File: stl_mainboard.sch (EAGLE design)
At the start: 5 parts, among them IC1 LM555D

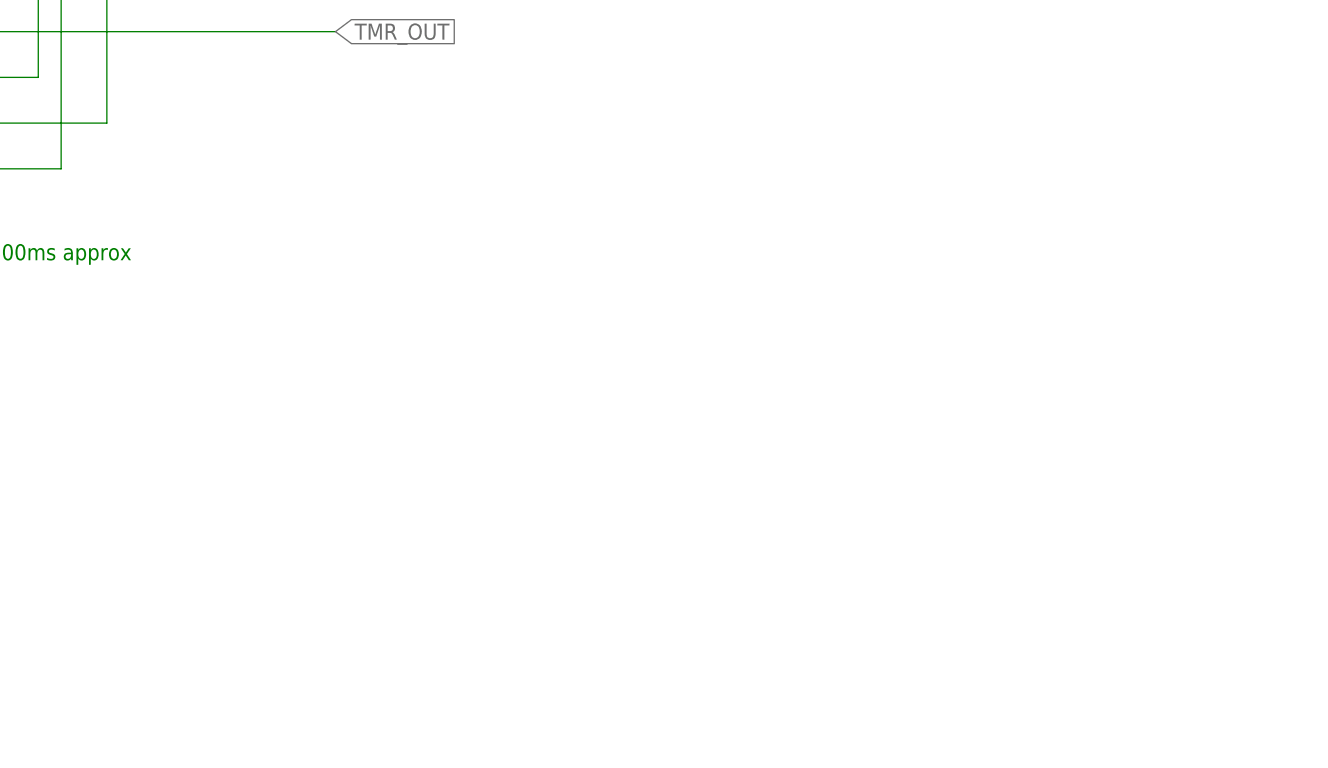
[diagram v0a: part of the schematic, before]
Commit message: Adds basicaly 555 timer schematic for 300ms period TODO: * develop 5V power supply * develop revers voltage protection * develop fuse * develop antistatic protection * develop MOSFET-base load control
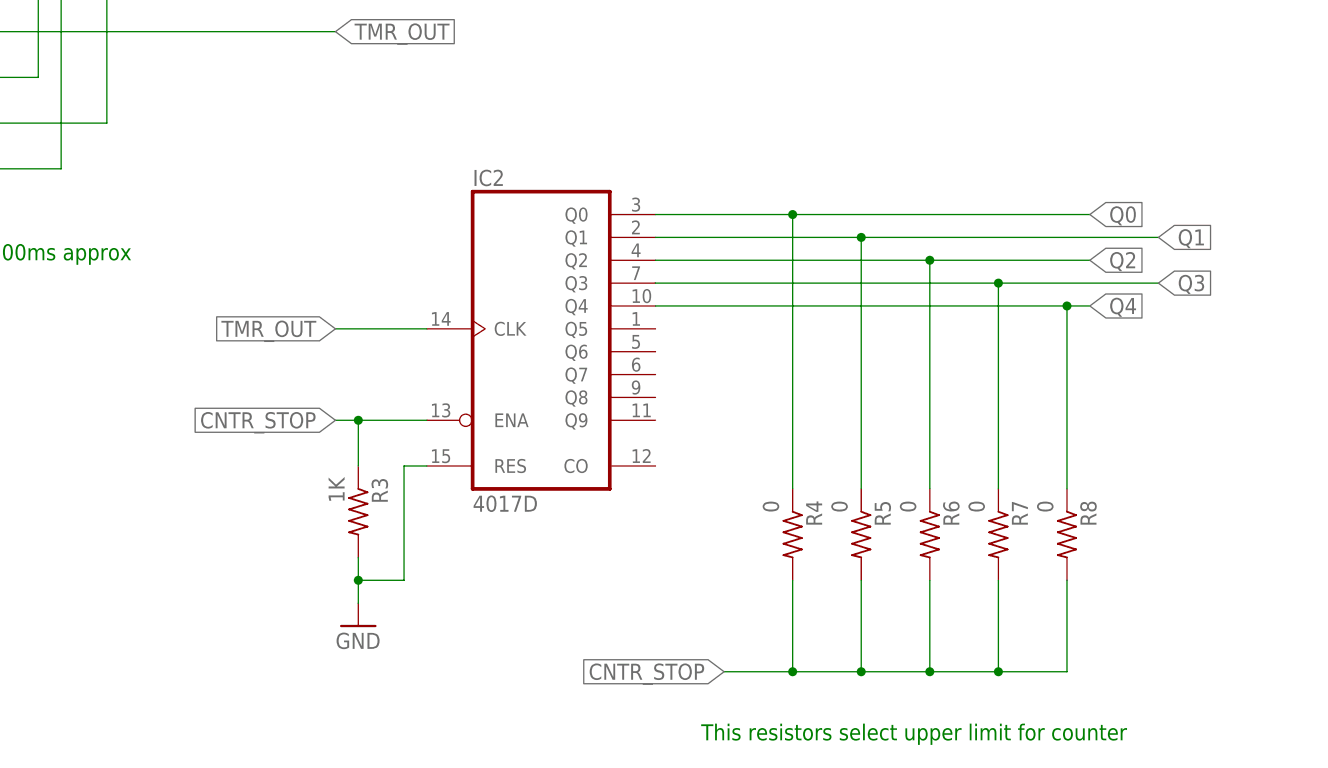
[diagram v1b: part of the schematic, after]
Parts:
- added IC2: 4017D, 40xx:4017D
- added R3: 1K, rcl:R-US_M1206
- added R4, R5, R6, R7, R8: 0, rcl:R-US_M1206
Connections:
- net +5V renamed VDD
- new net CNTR_STOP: IC2A.ENA, R3.1, R4.2, R5.2, R6.2, R7.2, R8.2
- new net Q0: IC2A.Q0, R4.1
- new net Q1: IC2A.Q1, R5.1
- new net Q2: IC2A.Q2, R6.1
- new net Q3: IC2A.Q3, R7.1
- new net Q4: IC2A.Q4, R8.1
- new net VSS: C1.-, C2.2, IC1.GND
- net GND: now also IC2A.RES, R3.2; no longer C1.-, C2.2, IC1.GND
- net TMR_OUT: now also IC2A.CLK
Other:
- note added: "This resistors select upper limit for counter"
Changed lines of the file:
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@@
 <part name="R1" library="rcl" deviceset="R-US_" device="M1206" value="1K"/>
 <part name="R2" library="rcl" deviceset="R-US_" device="M1206" value="4K2"/>
+<part name="IC2" library="40xx" deviceset="4017" device="D"/>
+<part name="R3" library="rcl" deviceset="R-US_" device="M1206" value="1K"/>
+<part name="GND2" library="supply1" deviceset="GND" device=""/>
+<part name="R4" library="rcl" deviceset="R-US_" device="M1206" value="0"/>
+<part name="R5" library="rcl" deviceset="R-US_" device="M1206" value="0"/>
+<part name="R6" library="rcl" deviceset="R-US_" device="M1206" value="0"/>
+<part name="R7" library="rcl" deviceset="R-US_" device="M1206" value="0"/>
+<part name="R8" library="rcl" deviceset="R-US_" device="M1206" value="0"/>
 </parts>
 <sheets>
@@
 <plain>
 <text x="-5.08" y="33.02" size="1.778" layer="91">Tiimer period must be 300ms approx</text>
+<text x="99.06" y="-20.32" size="1.778" layer="91">This resistors select upper limit for counter</text>
 </plain>
 <instances>
@@
 <instance part="R1" gate="G$1" x="5.08" y="76.2" rot="R180"/>
 <instance part="R2" gate="G$1" x="5.08" y="66.04" rot="R180"/>
+<instance part="IC2" gate="A" x="81.28" y="25.4"/>
+<instance part="R3" gate="G$1" x="60.96" y="5.08" rot="R270"/>
+<instance part="GND2" gate="1" x="60.96" y="-7.62"/>
+<instance part="R4" gate="G$1" x="109.22" y="2.54" rot="R270"/>
+<instance part="R5" gate="G$1" x="116.84" y="2.54" rot="R270"/>
+<instance part="R6" gate="G$1" x="124.46" y="2.54" rot="R270"/>
+<instance part="R7" gate="G$1" x="132.08" y="2.54" rot="R270"/>
+<instance part="R8" gate="G$1" x="139.7" y="2.54" rot="R270"/>
 </instances>
 <busses>
 </busses>
 <nets>
-<net name="+5V" class="0">
+<net name="VDD" class="0">
 <segment>
 <pinref part="P+2" gate="1" pin="+5V"/>
@@
 </segment>
 </net>
-<net name="GND" class="0">
+<net name="VSS" class="0">
 <segment>
 <pinref part="GND1" gate="1" pin="GND"/>
@@
 <wire x1="17.78" y1="58.42" x2="58.42" y2="58.42" width="0.1524" layer="91"/>
 <label x="58.42" y="58.42" size="1.778" layer="95" xref="yes"/>
+</segment>
+<segment>
+<pinref part="IC2" gate="A" pin="CLK"/>
+<wire x1="68.58" y1="25.4" x2="58.42" y2="25.4" width="0.1524" layer="91"/>
+<label x="58.42" y="25.4" size="1.778" layer="95" rot="R180" xref="yes"/>
 </segment>
 </net>
@@
 </segment>
 </net>
+<net name="CNTR_STOP" class="0">
+<segment>
+<pinref part="IC2" gate="A" pin="ENA"/>
+<pinref part="R3" gate="G$1" pin="1"/>
+<wire x1="68.58" y1="15.24" x2="60.96" y2="15.24" width="0.1524" layer="91"/>
+<wire x1="60.96" y1="15.24" x2="60.96" y2="10.16" width="0.1524" layer="91"/>
+<wire x1="60.96" y1="15.24" x2="58.42" y2="15.24" width="0.1524" layer="91"/>
+<label x="58.42" y="15.24" size="1.778" layer="95" rot="R180" xref="yes"/>
+<junction x="60.96" y="15.24"/>
+</segment>
+<segment>
+<pinref part="R8" gate="G$1" pin="2"/>
+<wire x1="139.7" y1="-2.54" x2="139.7" y2="-12.7" width="0.1524" layer="91"/>
+<wire x1="139.7" y1="-12.7" x2="132.08" y2="-12.7" width="0.1524" layer="91"/>
+<pinref part="R4" gate="G$1" pin="2"/>
+<wire x1="132.08" y1="-12.7" x2="124.46" y2="-12.7" width="0.1524" layer="91"/>
+<wire x1="124.46" y1="-12.7" x2="116.84" y2="-12.7" width="0.1524" layer="91"/>
+<wire x1="116.84" y1="-12.7" x2="109.22" y2="-12.7" width="0.1524" layer="91"/>
+<wire x1="109.22" y1="-12.7" x2="101.6" y2="-12.7" width="0.1524" layer="91"/>
+<wire x1="109.22" y1="-2.54" x2="109.22" y2="-12.7" width="0.1524" layer="91"/>
+<pinref part="R5" gate="G$1" pin="2"/>
+<wire x1="116.84" y1="-2.54" x2="116.84" y2="-12.7" width="0.1524" layer="91"/>
+<pinref part="R6" gate="G$1" pin="2"/>
+<wire x1="124.46" y1="-2.54" x2="124.46" y2="-12.7" width="0.1524" layer="91"/>
+<pinref part="R7" gate="G$1" pin="2"/>
+<wire x1="132.08" y1="-2.54" x2="132.08" y2="-12.7" width="0.1524" layer="91"/>
+<junction x="109.22" y="-12.7"/>
+<junction x="116.84" y="-12.7"/>
+<junction x="124.46" y="-12.7"/>
+<junction x="132.08" y="-12.7"/>
+<label x="101.6" y="-12.7" size="1.778" layer="95" rot="R180" xref="yes"/>
+</segment>
+</net>
+<net name="GND" class="0">
+<segment>
+<pinref part="R3" gate="G$1" pin="2"/>
+<pinref part="GND2" gate="1" pin="GND"/>
+<wire x1="60.96" y1="0" x2="60.96" y2="-2.54" width="0.1524" layer="91"/>
+<pinref part="IC2" gate="A" pin="RES"/>
+<wire x1="60.96" y1="-2.54" x2="60.96" y2="-5.08" width="0.1524" layer="91"/>
+<wire x1="68.58" y1="10.16" x2="66.04" y2="10.16" width="0.1524" layer="91"/>
+<wire x1="66.04" y1="10.16" x2="66.04" y2="-2.54" width="0.1524" layer="91"/>
+<wire x1="66.04" y1="-2.54" x2="60.96" y2="-2.54" width="0.1524" layer="91"/>
+<junction x="60.96" y="-2.54"/>
+</segment>
+</net>
+<net name="Q0" class="0">
+<segment>
+<pinref part="IC2" gate="A" pin="Q0"/>
+<wire x1="93.98" y1="38.1" x2="109.22" y2="38.1" width="0.1524" layer="91"/>
+<pinref part="R4" gate="G$1" pin="1"/>
+<wire x1="109.22" y1="7.62" x2="109.22" y2="38.1" width="0.1524" layer="91"/>
+<junction x="109.22" y="38.1"/>
+<wire x1="109.22" y1="38.1" x2="142.24" y2="38.1" width="0.1524" layer="91"/>
+<label x="142.24" y="38.1" size="1.778" layer="95" xref="yes"/>
+</segment>
+</net>
+<net name="Q1" class="0">
+<segment>
+<pinref part="IC2" gate="A" pin="Q1"/>
+<wire x1="93.98" y1="35.56" x2="116.84" y2="35.56" width="0.1524" layer="91"/>
+<pinref part="R5" gate="G$1" pin="1"/>
+<wire x1="116.84" y1="7.62" x2="116.84" y2="35.56" width="0.1524" layer="91"/>
+<junction x="116.84" y="35.56"/>
+<wire x1="116.84" y1="35.56" x2="149.86" y2="35.56" width="0.1524" layer="91"/>
+<label x="149.86" y="35.56" size="1.778" layer="95" xref="yes"/>
+</segment>
+</net>
+<net name="Q2" class="0">
+<segment>
+<pinref part="IC2" gate="A" pin="Q2"/>
+<wire x1="93.98" y1="33.02" x2="124.46" y2="33.02" width="0.1524" layer="91"/>
+<pinref part="R6" gate="G$1" pin="1"/>
+<wire x1="124.46" y1="7.62" x2="124.46" y2="33.02" width="0.1524" layer="91"/>
+<junction x="124.46" y="33.02"/>
+<wire x1="124.46" y1="33.02" x2="142.24" y2="33.02" width="0.1524" layer="91"/>
+<label x="142.24" y="33.02" size="1.778" layer="95" xref="yes"/>
+</segment>
+</net>
+<net name="Q3" class="0">
+<segment>
+<pinref part="IC2" gate="A" pin="Q3"/>
+<wire x1="93.98" y1="30.48" x2="132.08" y2="30.48" width="0.1524" layer="91"/>
+<pinref part="R7" gate="G$1" pin="1"/>
+<wire x1="132.08" y1="7.62" x2="132.08" y2="30.48" width="0.1524" layer="91"/>
+<junction x="132.08" y="30.48"/>
+<wire x1="132.08" y1="30.48" x2="149.86" y2="30.48" width="0.1524" layer="91"/>
+<label x="149.86" y="30.48" size="1.778" layer="95" xref="yes"/>
+</segment>
+</net>
+<net name="Q4" class="0">
+<segment>
+<pinref part="IC2" gate="A" pin="Q4"/>
+<wire x1="93.98" y1="27.94" x2="139.7" y2="27.94" width="0.1524" layer="91"/>
+<pinref part="R8" gate="G$1" pin="1"/>
+<wire x1="139.7" y1="27.94" x2="142.24" y2="27.94" width="0.1524" layer="91"/>
+<wire x1="139.7" y1="7.62" x2="139.7" y2="27.94" width="0.1524" layer="91"/>
+<junction x="139.7" y="27.94"/>
+<label x="142.24" y="27.94" size="1.778" layer="95" xref="yes"/>
+</segment>
+</net>

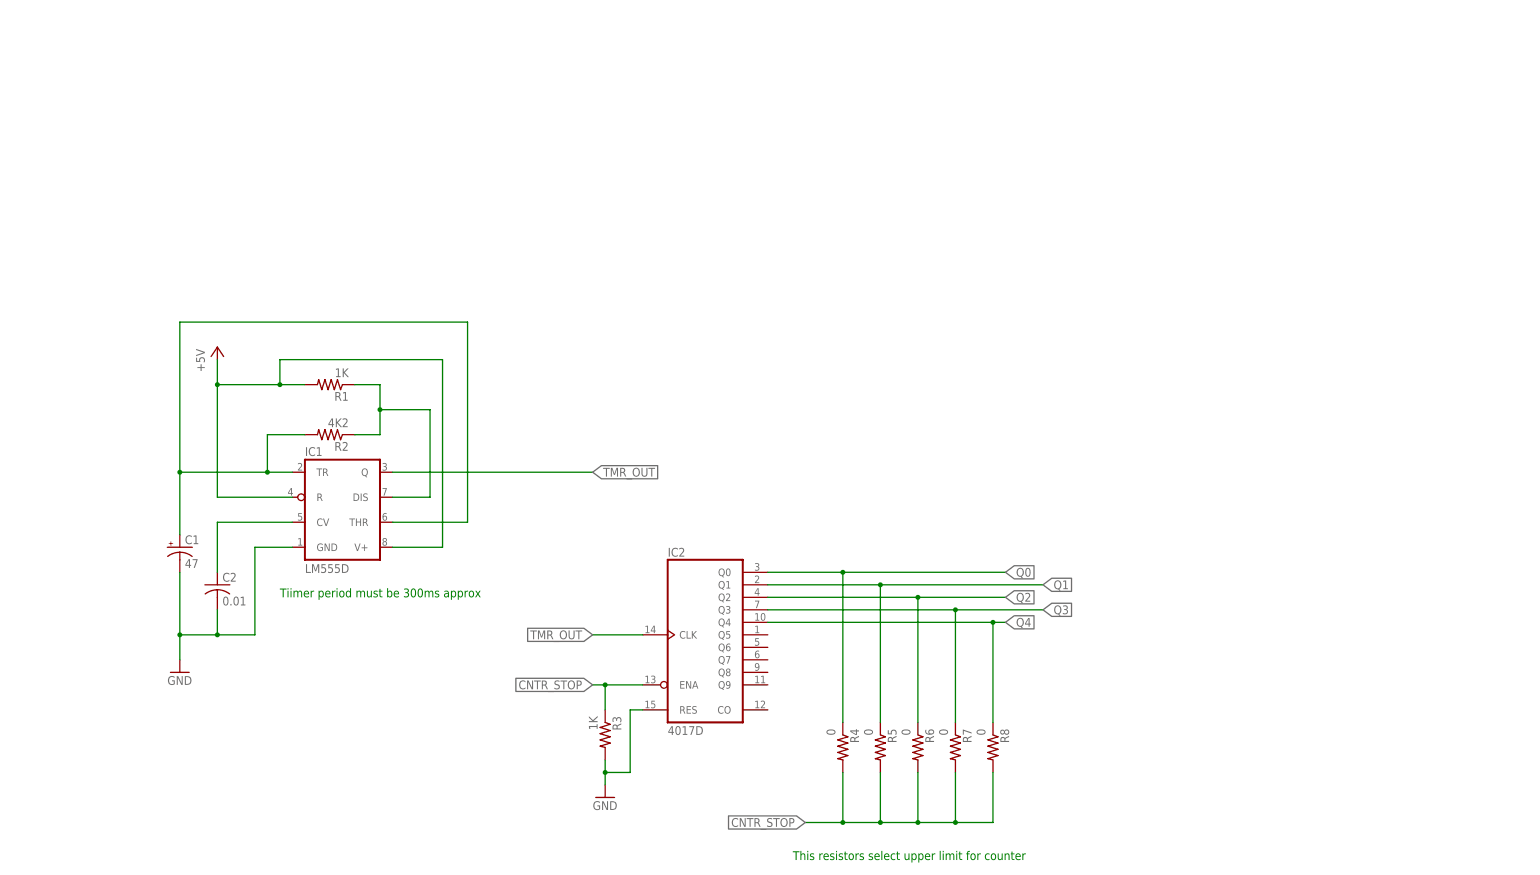
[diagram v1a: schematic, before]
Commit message: Adds power mosfets, removes unnecessary 7805 TODO: * develop revers voltage protection * develop fuse * develop antistatic protection
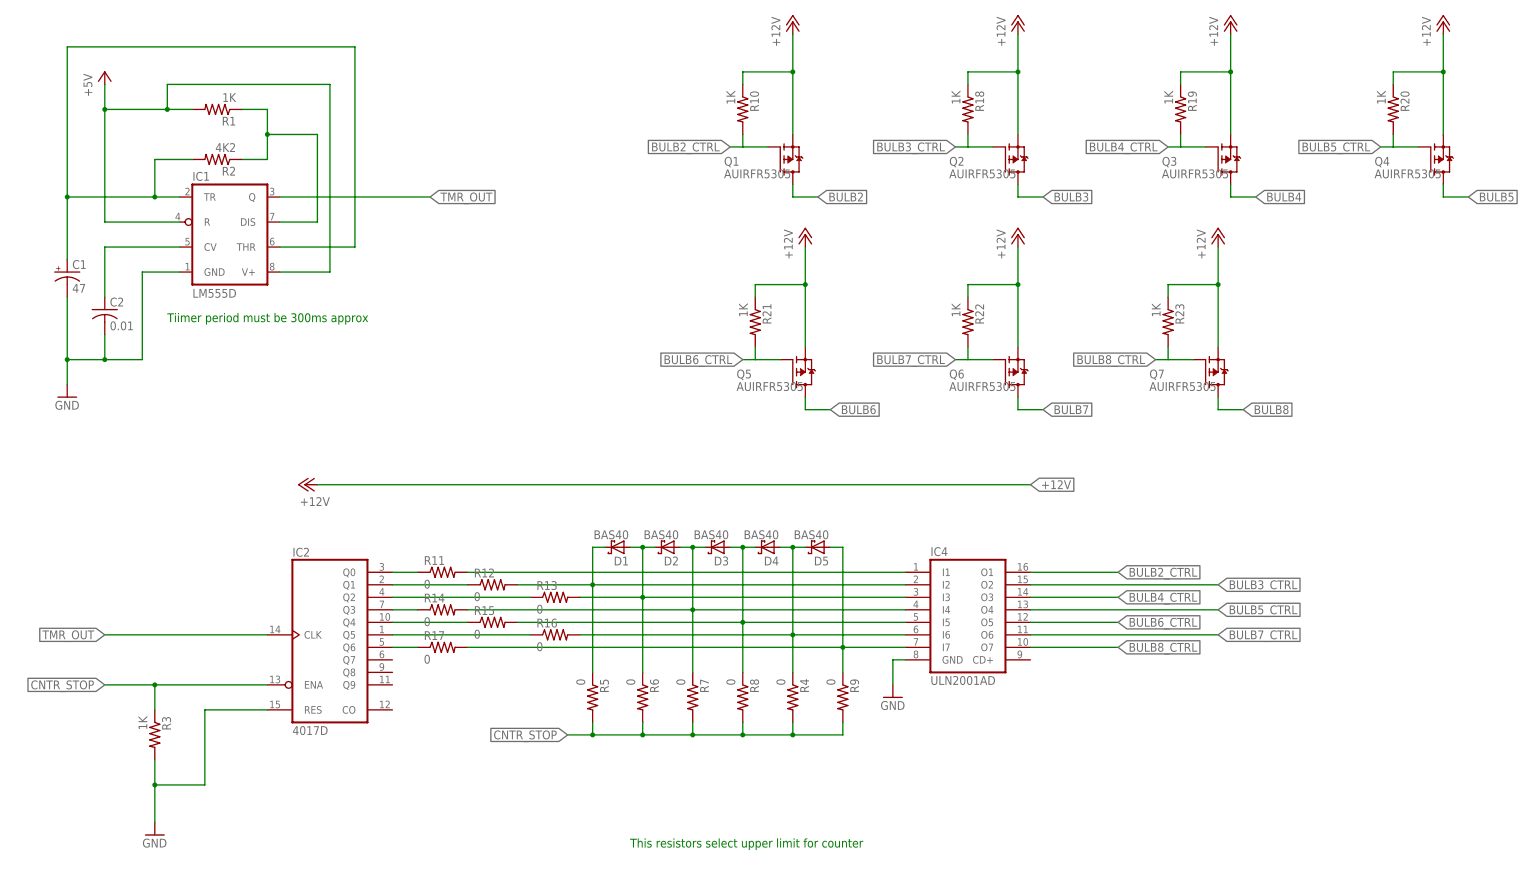
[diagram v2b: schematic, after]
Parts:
- added D1, D2, D3, D4, D5: BAS40, diode:BAS40
- added IC4: ULN2001AD, uln-udn:ULN2001AD
- added Q1, Q2, Q3, Q4, Q5, Q6, Q7: AUIRFR5305, transistor-fet:SPD30P06PTO252
- added R10, R18, R19, R20, R21, R22, R23: 1K, rcl:R-US_M1206
- added R11, R12, R13, R14, R15, R16, R17, R9: 0, rcl:R-US_M1206
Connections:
- new net +12V: Q1.S, Q2.S, Q3.S, Q4.S, Q5.S, Q6.S, Q7.S, R10.1, R18.1, R19.1, R20.1, R21.1, R22.1, R23.1
- new net BULB2: Q1.D
- new net BULB2_CTRL: IC4.O1, Q1.G, R10.2
- new net BULB3: Q2.D
- new net BULB3_CTRL: IC4.O2, Q2.G, R18.2
- new net BULB4: Q3.D
- new net BULB4_CTRL: IC4.O3, Q3.G, R19.2
- new net BULB5: Q4.D
- new net BULB5_CTRL: IC4.O4, Q4.G, R20.2
- new net BULB6: Q5.D
- new net BULB6_CTRL: IC4.O5, Q5.G, R21.2
- new net BULB7: Q6.D
- new net BULB7_CTRL: IC4.O6, Q6.G, R22.2
- new net BULB8: Q7.D
- new net BULB8_CTRL: IC4.O7, Q7.G, R23.2
- new net N$10: IC2A.Q6, R17.1
- new net N$4: IC2A.Q0, R11.1
- new net N$5: IC2A.Q1, R12.1
- new net N$6: IC2A.Q2, R13.1
- new net N$7: IC2A.Q3, R14.1
- new net N$8: IC2A.Q4, R15.1
- new net N$9: IC2A.Q5, R16.1
- new net Q5: D4.A, D5.C, IC4.I6, R16.2, R4.1
- new net Q6: D5.A, IC4.I7, R17.2, R9.1
- net CNTR_STOP: now also R9.2
- net GND: now also IC4.GND
- net Q0: now also IC4.I1, R11.2; no longer IC2A.Q0, R4.1
- net Q1: now also D1.C, IC4.I2, R12.2; no longer IC2A.Q1
- net Q2: now also D1.A, D2.C, IC4.I3, R13.2; no longer IC2A.Q2
- net Q3: now also D2.A, D3.C, IC4.I4, R14.2; no longer IC2A.Q3
- net Q4: now also D3.A, D4.C, IC4.I5, R15.2; no longer IC2A.Q4
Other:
- moved on the sheet: C1, C2, IC1, IC2, R1, R2, R3, R4, R5, R6, R7, R8

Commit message: WIP: input voltage spike and reverse protection
Also adds wago 508 screw connectors

TODO:
* develop fuse
* develop antistatic protection
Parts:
- added C3: 0.1uF, rcl:C-USC1206
- added D6: SMBJ15, diode:SUPPRESSOR-SMBJ
- added D7: 48CTQ060S, diode:BY229B
- added X1: (no value), con-wago-500:W237-102
- added X2: (no value), con-wago-508:W237-08P
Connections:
- new net N$11: D7.2, X1-1.KL
- net +12V: now also D6.C, D7.1, D7.K
- net GND: now also D6.A, X1-2.KL
- net VDD: now also C3.1
- net VSS: now also C3.2
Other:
- moved on the sheet: C1, C2, IC1, R1, R2, R3
